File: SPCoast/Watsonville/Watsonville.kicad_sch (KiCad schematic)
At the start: 126 parts, among them SW11 11, SW13 13, SW15 15, SW17 17, SW19 19, SW21 21, SW23 23, SW25 25, SW3 3, SW5 5, SW7 7, SW837 837, SW9 9

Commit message: fix(kicad): Watsonville auxiliary reference FLK becomes FLK2
A reference with no number makes kicad-cli report 'schematic has annotation
errors'; the GUI does not show it. Reference only, no railroad name changes.

Verified: kicad-cli netlist export of Watsonville prints no warning; 96 nets.

Co-Authored-By: Claude Sonnet 5.5 <noreply@anthropic.com>
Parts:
- renumbered FLK to FLK2
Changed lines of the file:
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@@
 		(in_pos_files yes)
 		(dnp no)
-		(property "Reference" "FLK"
+		(property "Reference" "FLK2"
 			(at 38.1 44.45 0)
 			(hide yes)
@@
 			(project "Watsonville"
 				(path "/773cfd5d-7233-47b3-8f6c-03be10f2d31c"
-					(reference "FLK")
+					(reference "FLK2")
 					(unit 1)
 				)

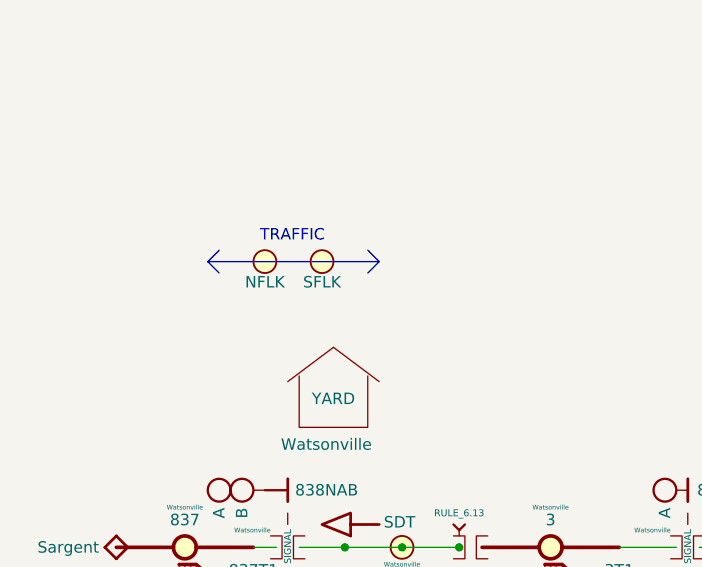
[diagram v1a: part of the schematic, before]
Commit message: SPCoast: owner's edit: Sargent HBA is an AUXILIARY appliance; Watsonville NFLK/SFLK are AUXILIARY_TRAFFIC (baseline)
Co-Authored-By: Claude Sonnet 5.5 <noreply@anthropic.com>
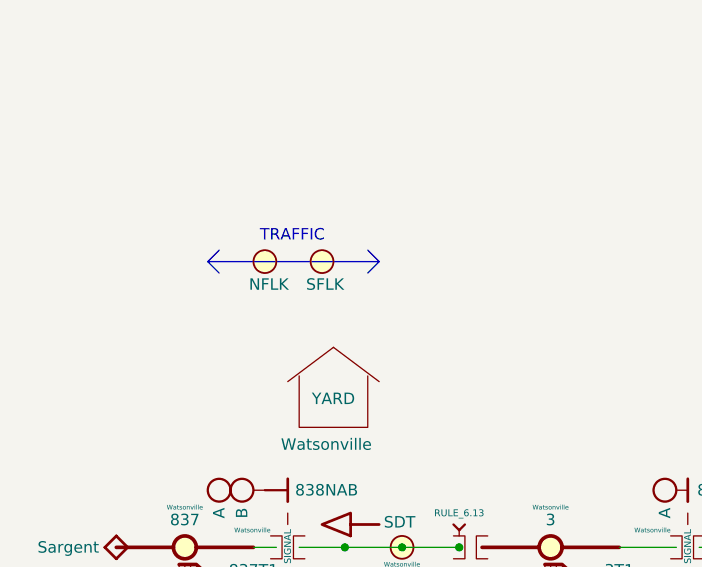
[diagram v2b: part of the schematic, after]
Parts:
- removed FLK1: SFLK, symbol Railroad:AUXILIARY
- removed FLK2: NFLK, symbol Railroad:AUXILIARY
- added FLK3: NFLK, symbol Railroad:AUXILIARY_TRAFFIC
- added FLK4: SFLK, symbol Railroad:AUXILIARY_TRAFFIC
- S10, S3, S4, S5, S6, S7, S8, S9: CP (none) -> Watsonville
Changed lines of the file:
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@@
 	)
 	(symbol
-		(lib_id "Railroad:AUXILIARY")
-		(at 38.1 41.91 0)
-		(unit 1)
-		(body_style 1)
-		(exclude_from_sim no)
-		(in_bom yes)
-		(on_board yes)
-		(in_pos_files yes)
-		(dnp no)
-		(property "Reference" "FLK2"
-			(at 38.1 44.45 0)
-			(hide yes)
-			(show_name no)
-			(do_not_autoplace yes)
-			(effects
-				(font
-					(size 1.27 1.27)
-				)
-			)
-		)
-		(property "Value" "NFLK"
-			(at 38.1 44.196 0)
-			(show_name no)
-			(do_not_autoplace no)
-			(effects
-				(font
-					(size 1.27 1.27)
-				)
-			)
-		)
-		(property "Footprint" ""
-			(at 38.1 41.91 0)
-			(hide yes)
-			(show_name no)
-			(do_not_autoplace no)
-			(effects
-				(font
-					(size 1.27 1.27)
-				)
-			)
-		)
-		(property "Datasheet" ""
-			(at 38.1 41.91 0)
-			(hide yes)
-			(show_name no)
-			(do_not_autoplace no)
-			(effects
-				(font
-					(size 1.27 1.27)
-				)
-			)
-		)
-		(property "Description" ""
-			(at 38.1 41.91 0)
-			(hide yes)
-			(show_name no)
-			(do_not_autoplace no)
-			(effects
-				(font
-					(size 1.27 1.27)
-				)
-			)
-		)
-		(property "Role" "APPLIANCE"
-			(at 38.1 41.91 0)
-			(hide yes)
-			(show_name no)
-			(do_not_autoplace no)
-			(effects
-				(font
-					(size 1.27 1.27)
-				)
-			)
-		)
-		(property "Kind" "AUXILIARY"
-			(at 38.1 41.91 0)
-			(hide yes)
-			(show_name no)
-			(do_not_autoplace no)
-			(effects
-				(font
-					(size 1.27 1.27)
-				)
-			)
-		)
-		(pin "1"
-		)
-		(instances
-			(project "Watsonville"
-				(path "/773cfd5d-7233-47b3-8f6c-03be10f2d31c"
-					(reference "FLK2")
-					(unit 1)
-				)
-			)
-		)
-	)
-	(symbol
 		(lib_id "Railroad:Switch_Powered_Small")
 		(at 69.85 73.66 0)
@@
 			)
 		)
+		(property "CP" "Watsonville"
+			(at 132.08 120.65 0)
+			(hide yes)
+			(show_name no)
+			(do_not_autoplace no)
+			(effects
+				(font
+					(size 1.27 1.27)
+				)
+			)
+		)
 		(pin "1"
 		)
@@
 			)
 		)
+		(property "CP" "Watsonville"
+			(at 85.09 69.85 0)
+			(hide yes)
+			(show_name no)
+			(do_not_autoplace no)
+			(effects
+				(font
+					(size 1.27 1.27)
+				)
+			)
+		)
 		(pin "1"
 		)
@@
 			)
 		)
+		(property "CP" "Watsonville"
+			(at 118.11 105.41 0)
+			(hide yes)
+			(show_name no)
+			(do_not_autoplace no)
+			(effects
+				(font
+					(size 1.27 1.27)
+				)
+			)
+		)
 		(pin "1"
 		)
@@
 			)
 		)
+		(property "CP" "Watsonville"
+			(at 95.25 82.55 0)
+			(hide yes)
+			(show_name no)
+			(do_not_autoplace no)
+			(effects
+				(font
+					(size 1.27 1.27)
+				)
+			)
+		)
 		(pin "1"
 		)
@@
 			)
 		)
+		(property "CP" "Watsonville"
+			(at 102.87 90.17 0)
+			(hide yes)
+			(show_name no)
+			(do_not_autoplace no)
+			(effects
+				(font
+					(size 1.27 1.27)
+				)
+			)
+		)
 		(pin "1"
 		)
@@
 	)
 	(symbol
+		(lib_id "Railroad:AUXILIARY_TRAFFIC")
+		(at 38.1 41.91 0)
+		(unit 1)
+		(body_style 1)
+		(exclude_from_sim no)
+		(in_bom yes)
+		(on_board yes)
+		(in_pos_files yes)
+		(dnp no)
+		(property "Reference" "FLK3"
+			(at 38.1 44.45 0)
+			(hide yes)
+			(show_name no)
+			(do_not_autoplace yes)
+			(effects
+				(font
+					(size 1.27 1.27)
+				)
+			)
+		)
+		(property "Value" "NFLK"
+			(at 36.322 44.45 0)
+			(show_name no)
+			(do_not_autoplace no)
+			(effects
+				(font
+					(size 1.27 1.27)
+				)
+				(justify left)
+			)
+		)
+		(property "Footprint" ""
+			(at 38.1 41.91 0)
+			(hide yes)
+			(show_name no)
+			(do_not_autoplace no)
+			(effects
+				(font
+					(size 1.27 1.27)
+				)
+			)
+		)
+		(property "Datasheet" ""
+			(at 38.1 41.91 0)
+			(hide yes)
+			(show_name no)
+			(do_not_autoplace no)
+			(effects
+				(font
+					(size 1.27 1.27)
+				)
+			)
+		)
+		(property "Description" ""
+			(at 38.1 41.91 0)
+			(hide yes)
+			(show_name no)
+			(do_not_autoplace no)
+			(effects
+				(font
+					(size 1.27 1.27)
+				)
+			)
+		)
+		(property "Role" "APPLIANCE"
+			(at 38.1 41.91 0)
+			(hide yes)
+			(show_name no)
+			(do_not_autoplace no)
+			(effects
+				(font
+					(size 1.27 1.27)
+				)
+			)
+		)
+		(property "Kind" "AUXILIARY_TRAFFIC"
+			(at 38.1 41.91 0)
+			(hide yes)
+			(show_name no)
+			(do_not_autoplace no)
+			(effects
+				(font
+					(size 1.27 1.27)
+				)
+			)
+		)
+		(property "CP" "Watsonville"
+			(at 38.1 41.91 0)
+			(hide yes)
+			(show_name no)
+			(do_not_autoplace no)
+			(effects
+				(font
+					(size 1.27 1.27)
+				)
+			)
+		)
+		(pin "1"
+		)
+		(instances
+			(project "Watsonville"
+				(path "/773cfd5d-7233-47b3-8f6c-03be10f2d31c"
+					(reference "FLK3")
+					(unit 1)
+				)
+			)
+		)
+	)
+	(symbol
 		(lib_id "Railroad:Track Circuit_Yellow")
 		(at 168.91 137.16 0)
@@
 			)
 		)
+		(property "CP" "Watsonville"
+			(at 110.49 97.79 0)
+			(hide yes)
+			(show_name no)
+			(do_not_autoplace no)
+			(effects
+				(font
+					(size 1.27 1.27)
+				)
+			)
+		)
 		(pin "1"
 		)
@@
 	)
 	(symbol
-		(lib_id "Railroad:AUXILIARY")
+		(lib_id "Railroad:AUXILIARY_TRAFFIC")
 		(at 44.45 41.91 0)
 		(unit 1)
@@
 		(in_pos_files yes)
 		(dnp no)
-		(property "Reference" "FLK1"
+		(property "Reference" "FLK4"
 			(at 44.45 44.45 0)
 			(hide yes)
@@
 		)
 		(property "Value" "SFLK"
-			(at 44.45 44.196 0)
+			(at 42.672 44.45 0)
 			(show_name no)
 			(do_not_autoplace no)
@@
 					(size 1.27 1.27)
 				)
+				(justify left)
 			)
 		)
@@
 			)
 		)
-		(property "Kind" "AUXILIARY"
+		(property "Kind" "AUXILIARY_TRAFFIC"
+			(at 44.45 41.91 0)
+			(hide yes)
+			(show_name no)
+			(do_not_autoplace no)
+			(effects
+				(font
+					(size 1.27 1.27)
+				)
+			)
+		)
+		(property "CP" "Watsonville"
 			(at 44.45 41.91 0)
 			(hide yes)
@@
 			(project "Watsonville"
 				(path "/773cfd5d-7233-47b3-8f6c-03be10f2d31c"
-					(reference "FLK1")
+					(reference "FLK4")
 					(unit 1)
 				)
@@
 			)
 		)
+		(property "CP" "Watsonville"
+			(at 245.11 140.97 0)
+			(hide yes)
+			(show_name no)
+			(do_not_autoplace no)
+			(effects
+				(font
+					(size 1.27 1.27)
+				)
+			)
+		)
 		(pin "1"
 		)
@@
 			(at 125.73 113.03 0)
 			(hide yes)
+			(show_name no)
+			(do_not_autoplace no)
+			(effects
+				(font
+					(size 1.27 1.27)
+				)
+			)
+		)
+		(property "CP" "Watsonville"
+			(at 125.73 113.03 0)
+			(hide yes)

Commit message: SPCoast: owner's edits: schematics synced with the revised symbol libraries (baseline)
Update Symbols from Library on all plant and desk sheets; CP values for
Christopher, GilroyInterchange and Luchessa; Restricted Speed markers
consolidated in Corporal, Luchessa and Sargent.

Observed in the diff, not changed by the sweep that follows: CP changed on 23
symbols (Christopher: prefix removed, 815/815A/IND now Christopher North) and
added on 12 (GilroyInterchange); two lamps' Color reset to their symbol variant
(Christopher LMP93 red -> yellow, Sargent LMP133 yellow -> red).

Verified: netlists keep their net counts (Christopher 33, Corporal 26,
GilroyCalTrain 27, GilroyInterchange 22, Luchessa 34, Sargent 18, Watsonville
96, South-cTc 341); desk compiles to 75 appliances, 137 bindings, 14 columns;
no root-UUID regression.

Co-Authored-By: Claude Sonnet 5.5 <noreply@anthropic.com>
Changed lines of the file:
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@@
 			)
 		)
-		(property "Description" ""
+		(property "Description" "Rule 251 (Track Signaled in One Direction): Governs movements on tracks where signals are only configured for  one direction.  Under this rule, signal indications supersede the superiority of trains for movements operating with the current of traffic.  Moving against this traffic direction requires explicit authority (such as a train order or track warrant)."
 			(at 43.815 78.105 0)
 			(hide yes)
@@
 		)
 		(property "CP" "Watsonville"
-			(at 38.735 71.755 0)
+			(at 40.64 76.2 0)
 			(show_name no)
 			(do_not_autoplace no)
@@
 					(color 72 72 72 1)
 				)
-				(justify right)
 			)
 		)
@@
 		)
 		(property "CP" "Watsonville"
-			(at 116.205 107.315 0)
+			(at 118.11 111.76 0)
 			(show_name no)
 			(do_not_autoplace no)
@@
 					(color 72 72 72 1)
 				)
-				(justify right)
 			)
 		)
@@
 		)
 		(property "CP" "Watsonville"
-			(at 45.085 84.455 0)
+			(at 46.99 88.9 0)
 			(show_name no)
 			(do_not_autoplace no)
@@
 					(color 72 72 72 1)
 				)
-				(justify right)
 			)
 		)
@@
 		)
 		(property "CP" "Watsonville"
-			(at 108.585 99.695 0)
+			(at 110.49 104.14 0)
 			(show_name no)
 			(do_not_autoplace no)
@@
 					(color 72 72 72 1)
 				)
-				(justify right)
 			)
 		)
@@
 			)
 		)
-		(property "Description" "Yard Limits: a designated section of the main track where trains and engines may operate without protecting against other movements,"
+		(property "Description" "Yard Limits: Standard Code Rule 93, GCOR RULE 6.13: a designated section of the main track where trains and engines may operate without protecting against other movements,"
 			(at 56.515 75.565 0)
 			(hide yes)
@@
 		)
 		(property "CP" "Watsonville"
-			(at 100.965 92.075 0)
+			(at 102.87 96.52 0)
 			(show_name no)
 			(do_not_autoplace no)
@@
 					(color 72 72 72 1)
 				)
-				(justify right)
 			)
 		)
@@
 		)
 		(property "CP" "Watsonville"
-			(at 247.015 139.065 0)
+			(at 245.11 134.62 0)
 			(show_name no)
 			(do_not_autoplace no)
@@
 					(color 72 72 72 1)
 				)
-				(justify right)
 			)
 		)
@@
 		)
 		(property "CP" "Watsonville"
-			(at 83.185 71.755 0)
+			(at 85.09 76.2 0)
 			(show_name no)
 			(do_not_autoplace no)
@@
 					(color 72 72 72 1)
 				)
-				(justify right)
 			)
 		)
@@
 		)
 		(property "CP" "Watsonville"
-			(at 130.175 122.555 0)
+			(at 132.08 127 0)
 			(show_name no)
 			(do_not_autoplace no)
@@
 					(color 72 72 72 1)
 				)
-				(justify right)
 			)
 		)
@@
 			)
 		)
-		(property "Description" "Maintainer Bungalow"
-			(at 45.72 62.87 0)
+		(property "Description" "Rrepresents the Control Point Maintainer Bungalow (plus optional Maintainer Call)"
+			(at 45.72 62.865 0)
 			(hide yes)
 			(show_name no)
@@
 		)
 		(property "CP" "Watsonville"
-			(at 93.345 84.455 0)
+			(at 95.25 88.9 0)
 			(show_name no)
 			(do_not_autoplace no)
@@
 					(color 72 72 72 1)
 				)
-				(justify right)
 			)
 		)
@@
 			)
 		)
-		(property "Description" ""
+		(property "Description" "Rule 251 (Track Signaled in One Direction): Governs movements on tracks where signals are only configured for  one direction.  Under this rule, signal indications supersede the superiority of trains for movements operating with the current of traffic.  Moving against this traffic direction requires explicit authority (such as a train order or track warrant)."
 			(at 102.235 141.605 0)
 			(hide yes)
@@
 		)
 		(property "CP" "Watsonville"
-			(at 123.825 114.935 0)
+			(at 125.73 119.38 0)
 			(show_name no)
 			(do_not_autoplace no)
@@
 					(color 72 72 72 1)
 				)
-				(justify right)
 			)
 		)
@@
 			)
 		)
-		(property "Description" "Yard Limits: a designated section of the main track where trains and engines may operate without protecting against other movements,"
+		(property "Description" "Yard Limits: Standard Code Rule 93, GCOR RULE 6.13: a designated section of the main track where trains and engines may operate without protecting against other movements,"
 			(at 56.515 97.155 0)
 			(hide yes)
@@
 		)
 		(property "Value" "Sargent"
-			(at 19.685 73.66 0)
+			(at 21.59 69.85 0)
 			(show_name no)
 			(do_not_autoplace no)
@@
 					(color 0 0 0 1)
 				)
-				(justify right)
 			)
 		)

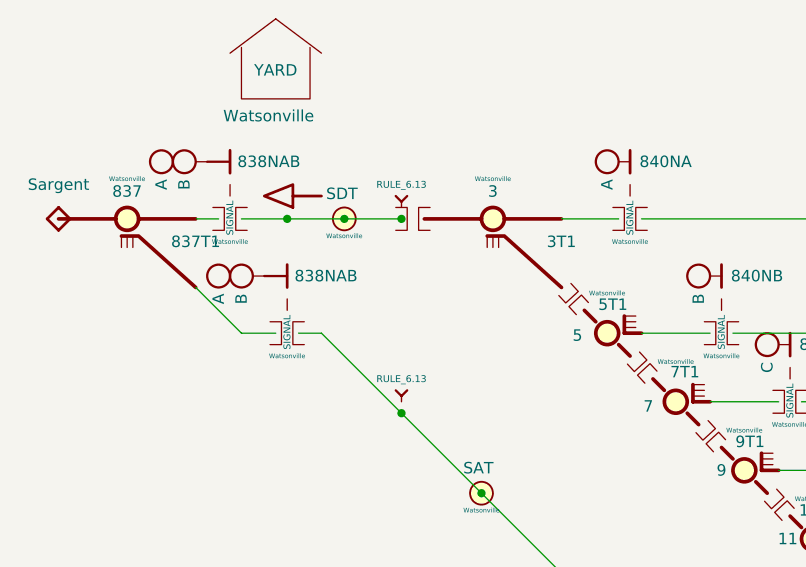
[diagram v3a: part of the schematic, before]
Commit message: chore(kicad): sweep instance Role/Kind and stale fields to the library vocabulary
Scripted, one pass over every sheet except Watsonville (open in KiCad, locked):
- Role/Kind of placed symbols refreshed from the library by lib_id: 10 Role
  (MAIN HOUSE CONTROLLED_POINT -> CONTROL_POINT, Rule251-DoT empty) and 17 Kind
  (IRJ-Signal IRJ -> IRJ_SIGNAL x7, Mast_Single/Double swaps, HandThrow
  -> SWITCH_MANUAL, Derail, PanelLock -> LOCK_LEVER, NextCP).
- Stale instance fields dropped where the library no longer has them: 39 Name,
  28 Direction (all empty or retired), 5 CP on Bumper and IRJ symbols.
- Orphan embedded copies of the retired symbol Rule6.28-OtherThanMain removed
  from two sheets (unused).

Not done: Watsonville (locked); CMRInet -> CMRI (library Kind still CMRInet);
fields new to the library (MAIN HOUSE Kind, switch Indications) are not copied
onto instances, the compiler will read library defaults by lib_id; Rulebook
fields stay until the compiler stops requiring them.

Verified: per-symbol before/after comparison shows only these changes, same
symbol sets, positions and lib_ids; netlists keep their net counts (Christopher
33, Corporal 26, GilroyCalTrain 27, GilroyInterchange 22, Luchessa 34, Sargent
18, South-cTc 341); desk still 75 appliances, 137 bindings, 14 columns.

Co-Authored-By: Claude Sonnet 5.5 <noreply@anthropic.com>
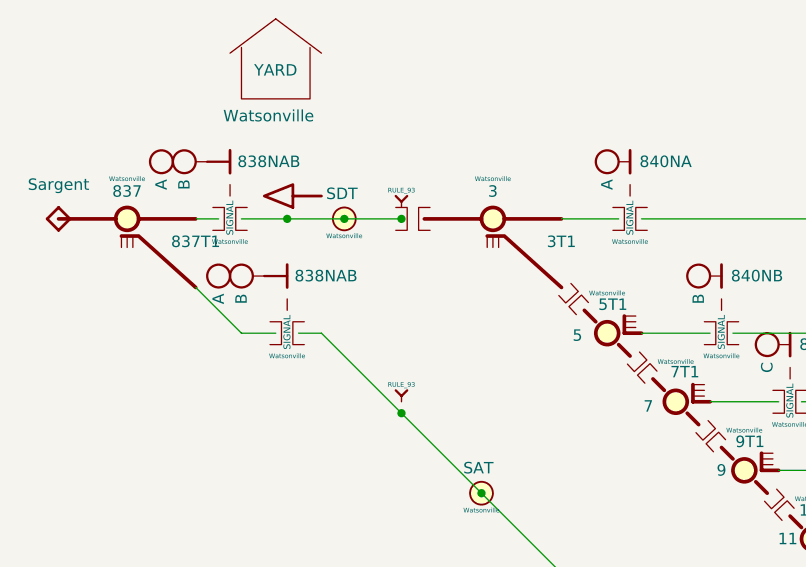
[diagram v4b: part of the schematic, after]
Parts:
- DOT1, DOT2: Kind RULE_6.13 -> RULE_93
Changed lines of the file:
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@@
 			)
 		)
-		(property "Kind" "RULE_6.13"
-			(at 59.69 69.85 0)
+		(property "Kind" "RULE_93"
+			(at 59.69 70.485 0)
 			(show_name no)
 			(do_not_autoplace yes)
 			(effects
 				(font
-					(size 0.762 0.762)
+					(size 0.508 0.508)
 				)
 			)
@@
 			)
 		)
-		(property "Kind" "RULE_6.13"
-			(at 59.69 91.44 0)
+		(property "Kind" "RULE_93"
+			(at 59.69 92.075 0)
 			(show_name no)
 			(do_not_autoplace yes)
 			(effects
 				(font
-					(size 0.762 0.762)
+					(size 0.508 0.508)
 				)
 			)

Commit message: chore(kicad): sweep Watsonville to the library vocabulary
Same scripted pass as the previous commit, now that Watsonville is closed:
2 Role and 2 Kind refreshed (Rule251-DoT markers with empty Role/Kind), 3 stale
Name fields and 32 stale CP fields on IRJ symbols dropped, 1 orphan embedded
Rule6.28-OtherThanMain removed.

Note: the previous commit (b2f035a) also contains the owner's own Watsonville
edit saved at 11:05 (the two Yard Limits markers RULE_6.13 -> RULE_93); its
message says Watsonville was excluded, which was true of the sweep only.

Verified: per-symbol before/after comparison shows only these changes, 126
symbols, positions and lib_ids unchanged; netlist 96 nets.

Co-Authored-By: Claude Sonnet 5.5 <noreply@anthropic.com>
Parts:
- B19, B20, B21, B22, B23, B24, B25, B26, B27, B28, B29, B30, B31, B32, B33, B34, B35, B36, B37, B38, B39, B4, B40, B41, B42, B44, B45, B46, B47, B48, B49, B6: CP Watsonville -> (none)
- DOT1, DOT2: Name Yard Limits -> (none)
- DOT3, DOT4: Kind (none) -> RULE_251; Role (none) -> POLICY

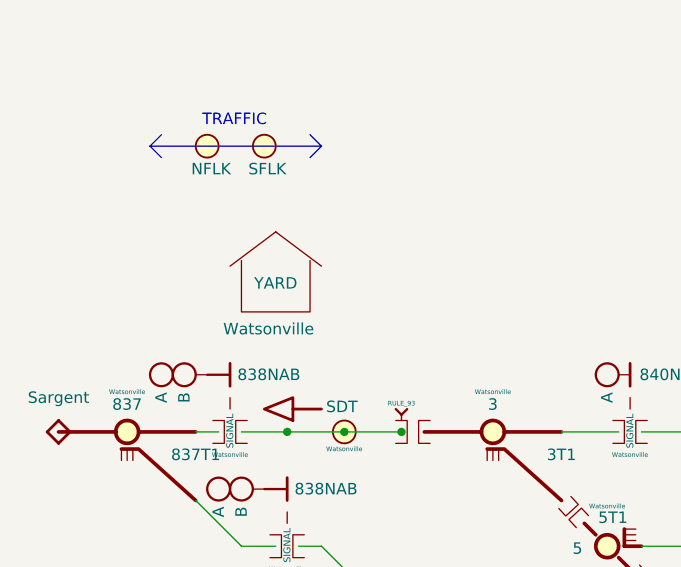
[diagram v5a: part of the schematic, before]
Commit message: SPCoast: owner's edits: Christopher OS lamps 813T1 and 817T1 use the red variant; Watsonville MAIN HOUSE LABEL removed (baseline)
Co-Authored-By: Claude Sonnet 5.5 <noreply@anthropic.com>
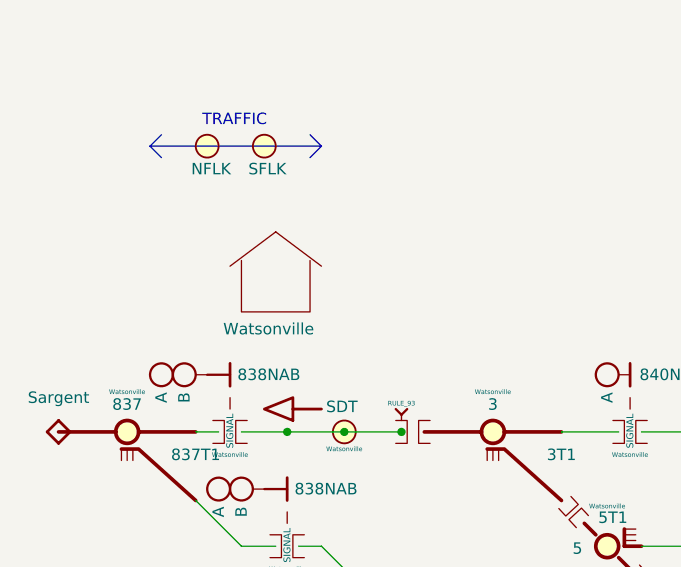
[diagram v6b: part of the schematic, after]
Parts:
- HOUSE1: LABEL YARD -> (none)
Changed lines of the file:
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@@
-			)
-		)
-		(property "LABEL" "YARD"
-			(at 45.72 57.15 0)
-			(show_name no)
-			(do_not_autoplace no)
-			(effects
-				(font
-					(size 1.27 1.27)
-				)
 			)
 		)
